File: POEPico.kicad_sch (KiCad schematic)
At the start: 0 parts

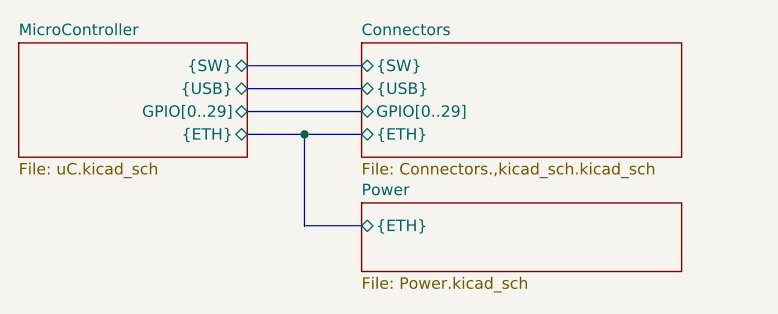
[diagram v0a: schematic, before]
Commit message: BOM Cleanup and matching for JLCPCB, downstream edits to Schematic and Board. Added backup files to .gitignore.
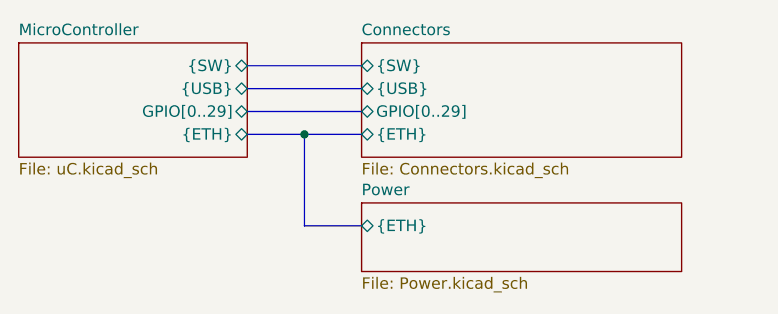
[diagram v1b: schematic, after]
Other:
- sheet Connectors: file Connectors.,kicad_sch.kicad_sch -> Connectors.kicad_sch
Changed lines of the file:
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@@
 			)
 		)
-		(property "Sheetfile" "Connectors.,kicad_sch.kicad_sch"
+		(property "Sheetfile" "Connectors.kicad_sch"
 			(at 127 64.0846 0)
 			(effects
